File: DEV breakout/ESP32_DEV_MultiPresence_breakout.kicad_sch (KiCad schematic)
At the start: 14 parts, among them J1 USB_C_Receptacle_Power, J2 JST_SH_01X04, U1 ESP32_DevKit_V1_DOIT, U2 EKMxxxxxxxxx, U3 SEN0395, U4 SEN0395

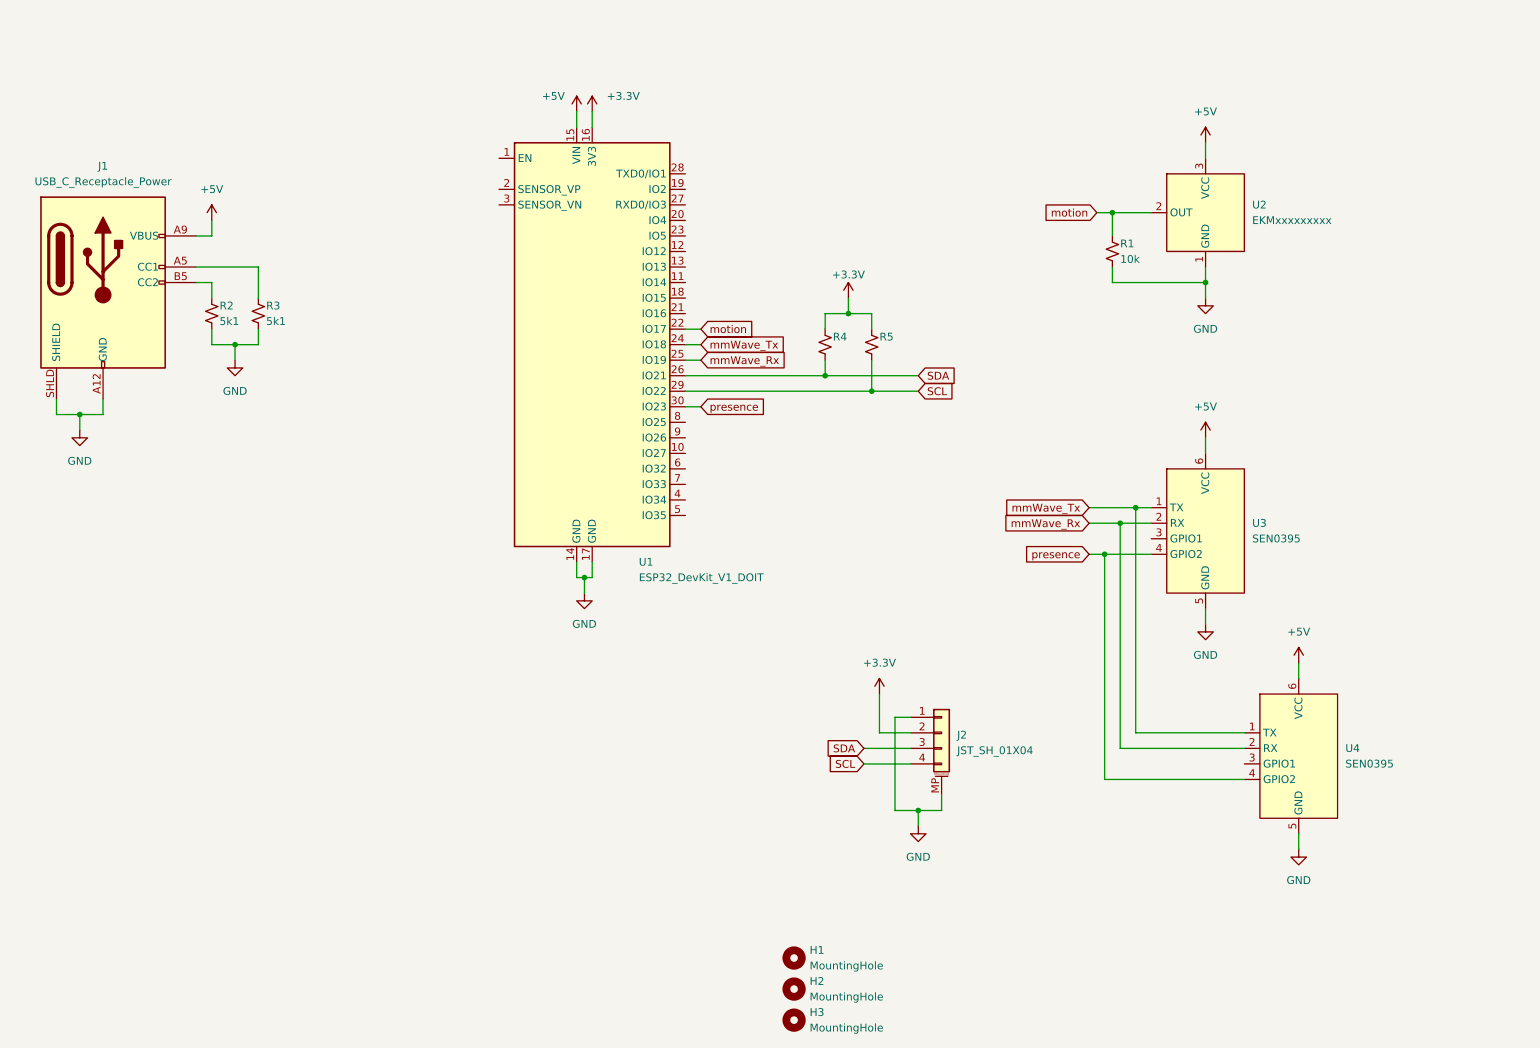
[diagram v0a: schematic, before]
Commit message: moved 5V line to let more GND thermal connections on the radar
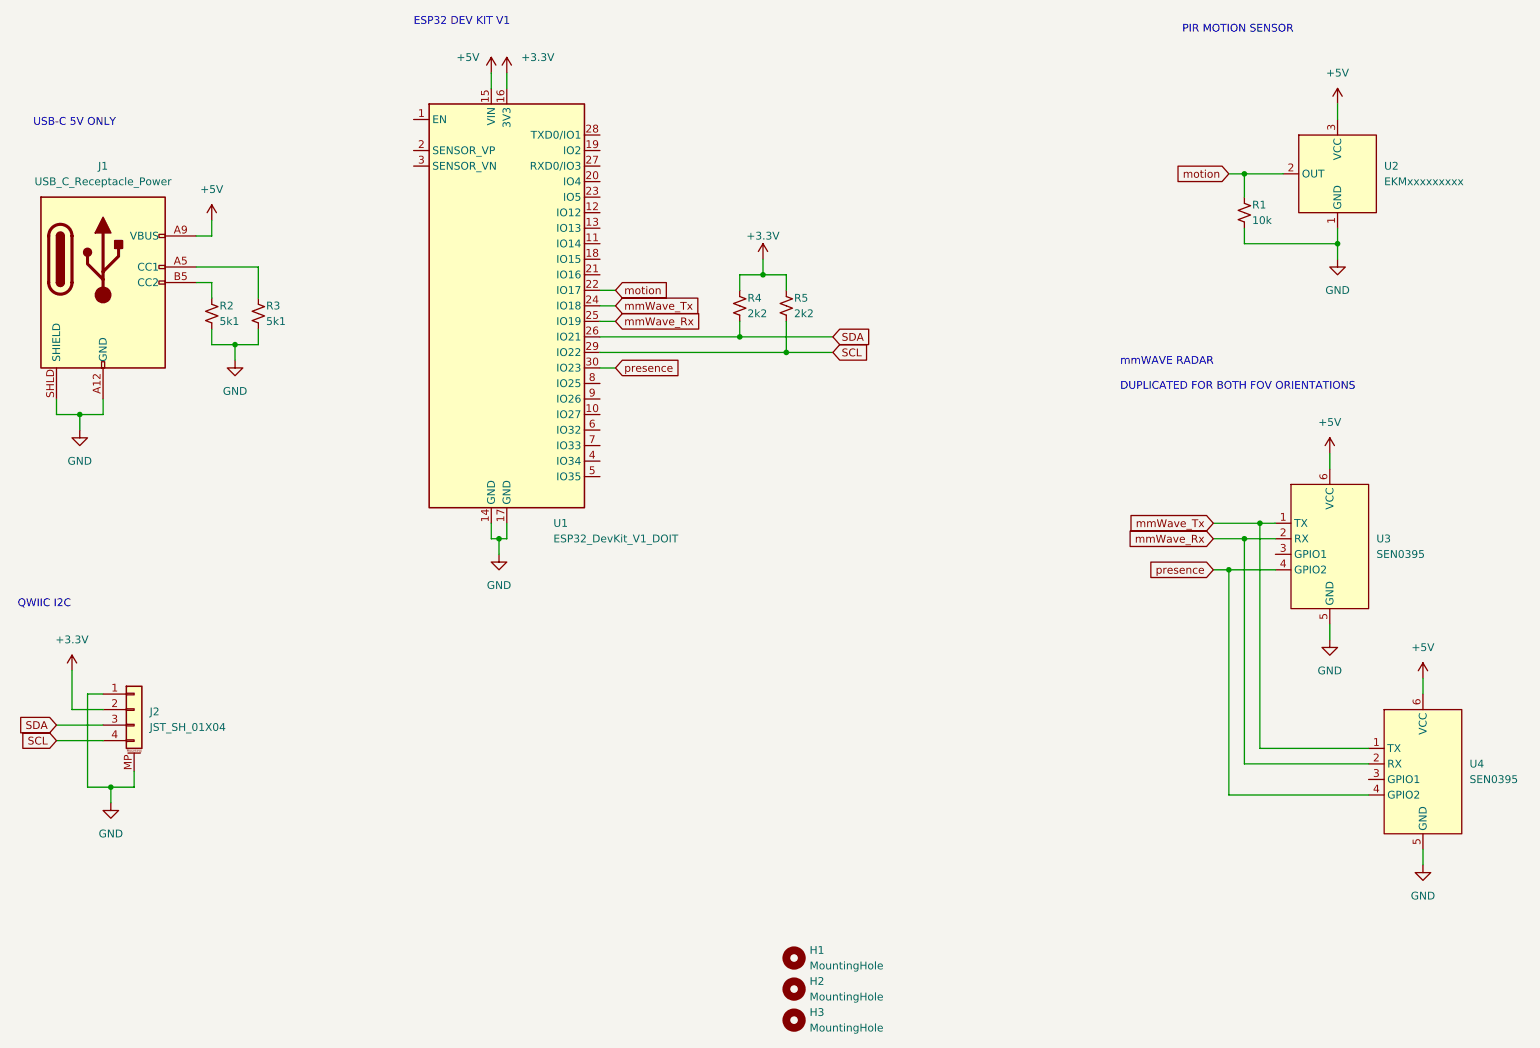
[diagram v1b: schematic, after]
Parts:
- R4, R5: value (none) -> 2k2
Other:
- note added: "ESP32 DEV KIT V1"
- note added: "PIR MOTION SENSOR"
- note added: "QWIIC I2C"
- note added: "USB-C 5V ONLY"
- note added: "mmWAVE RADAR DUPLICATED FOR BOTH FOV ORIENTATIONS"
- moved on the sheet: J2, R1, R4, R5, U1, U2, U3, U4
